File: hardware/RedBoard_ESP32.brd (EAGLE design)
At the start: 68.6 x 58.4 mm, 206 parts, among them J1 5.5x2.1mm Barrel, J13 QWIIC_RIGHT_ANGLE, J15 MICRO-SD-PUSH-PUSH-EXT-PIN, J2 USB C, J3 USB_SOLDER_PADS, J5 M10NO_SILK, Q1 MBT3904DW1T1, Q11 20V/4.2A/52mΩ/1.4W, Q13 20V/4.2A/52mΩ/1.4W, Q3 20V/4.2A/52mΩ/1.4W, Q5 20V/4.2A/52mΩ/1.4W, Q7 20V/4.2A/52mΩ/1.4W, Q9 20V/4.2A/52mΩ/1.4W, U1 ESP-WROOM-3232D-NARROW, U2 CH340C, U3 LM1117, U4 3.3V, U5 MCP73831, U6 MAX17048

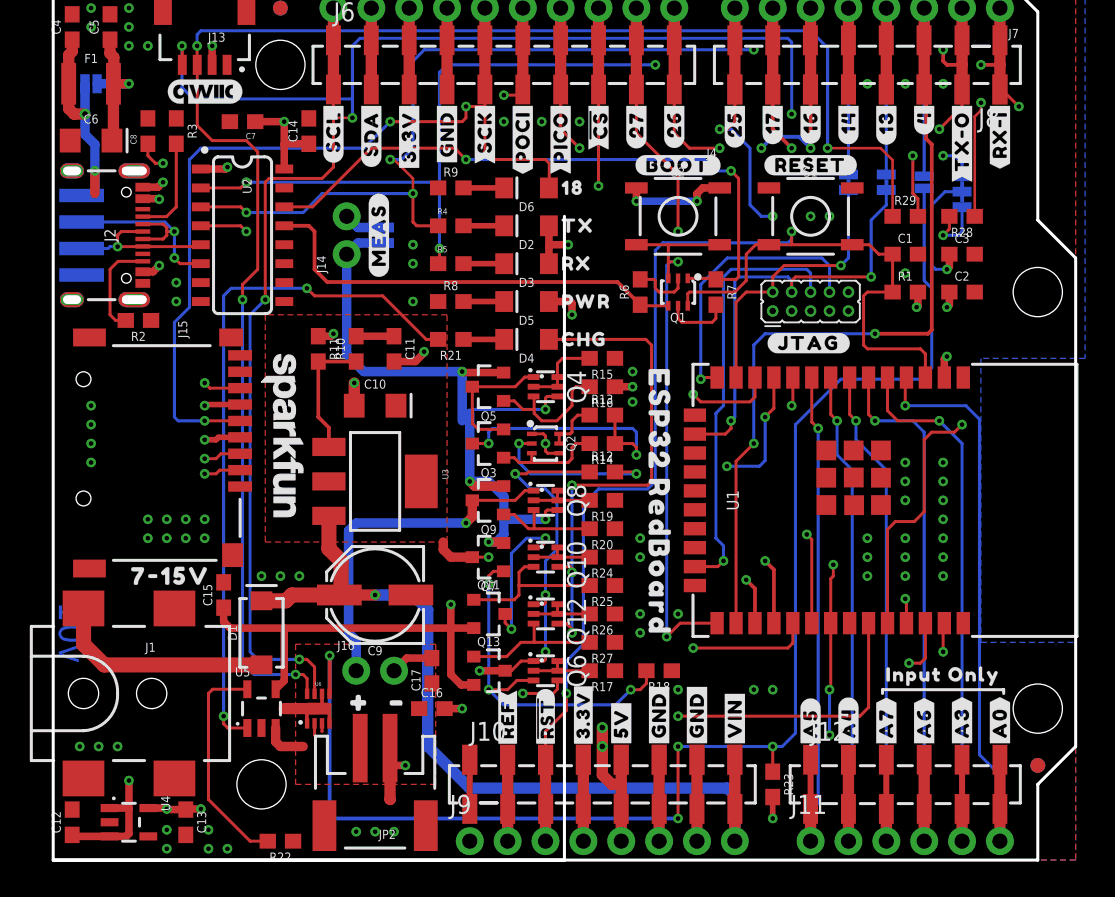
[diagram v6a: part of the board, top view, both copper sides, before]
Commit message: Moved SD card connector; updated RST/RESET flags.
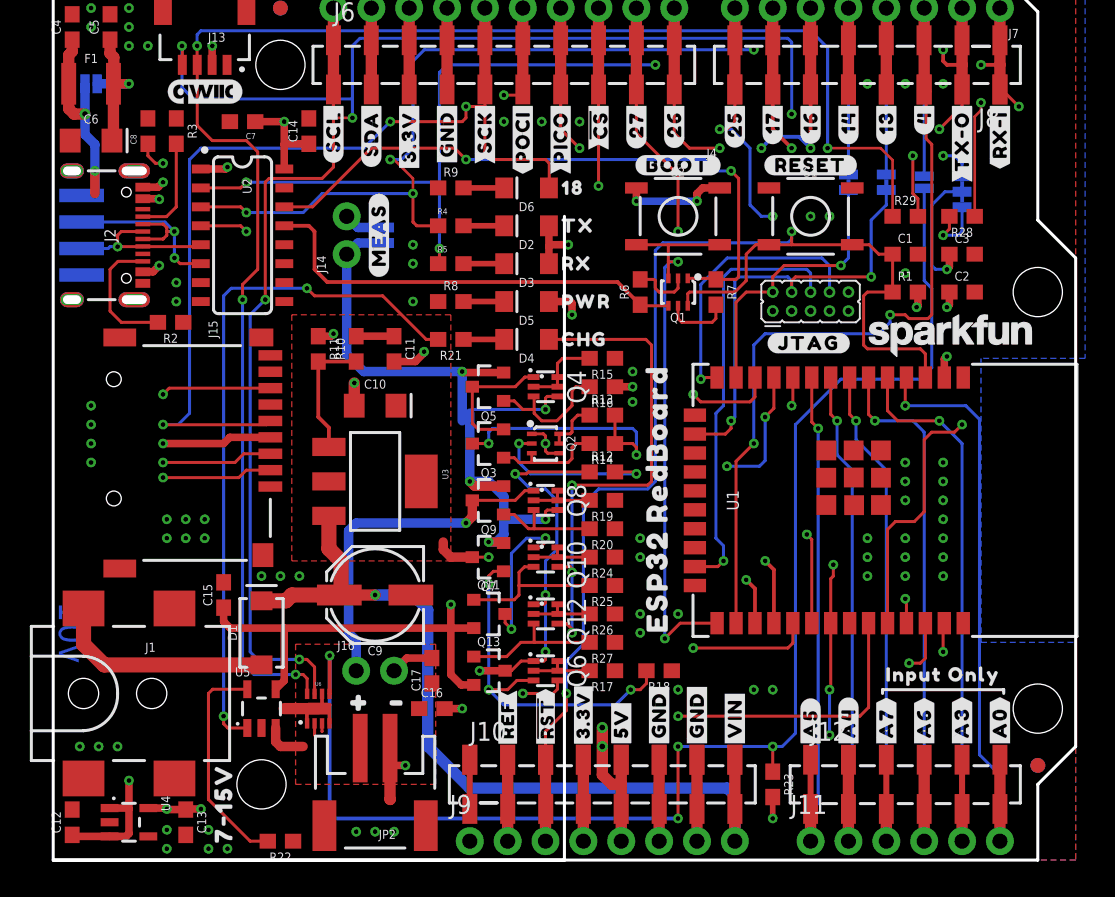
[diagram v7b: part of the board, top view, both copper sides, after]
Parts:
- moved LOGO1 45.3 mm to (60.2, 35.2), turned to 0 degrees
- moved U$48 19.8 mm to (40.5, 14.2), turned to 90 degrees
- moved U$49 15.6 mm to (11.4, 3.81), turned to 90 degrees
- moved U$47 5.08 mm to (40.5, 21.6), turned to 90 degrees
- moved R2 2.16 mm to (7.87, 36.1)
- moved J15 2.03 mm to (4.06, 27.3)
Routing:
- net ESP32_GPIO23_PICO: track 114.5 -> 122.7 mm
- net ESP32_GPIO5_!CS!: track 104.7 -> 112.4 mm
- net 3.3V: track 50.4 -> 55.4 mm
- net ESP32_GPIO18_SCK: track 115.9 -> 120.1 mm
- net GND: track 53.0 -> 50.6 mm, vias 83 -> 80
- net CC2: track 6.68 -> 8.75 mm
- net ESP32_GPIO19_POCI: track 149.6 -> 148.5 mm
